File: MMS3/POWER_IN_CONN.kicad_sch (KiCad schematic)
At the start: 1 part, among them J2 AMASS XT60

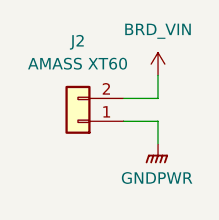
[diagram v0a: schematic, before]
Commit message: schematic + partly layout
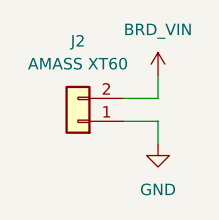
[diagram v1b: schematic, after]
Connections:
- net GNDPWR renamed GND
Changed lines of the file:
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@@
+	)
+	(symbol
+		(lib_id "power:GND")
+		(at 154.94 109.22 0)
+		(unit 1)
+		(body_style 1)
+		(exclude_from_sim no)
+		(in_bom yes)
+		(on_board yes)
+		(in_pos_files yes)
+		(dnp no)
+		(fields_autoplaced yes)
+		(property "Reference" "#PWR059"
+			(at 154.94 115.57 0)
+			(hide yes)
+			(show_name no)
+			(do_not_autoplace no)
+			(effects
+				(font
+					(size 1.27 1.27)
+				)
+			)
+		)
+		(property "Value" "GND"
+			(at 154.94 114.3 0)
+			(show_name no)
+			(do_not_autoplace no)
+			(effects
+				(font
+					(size 1.27 1.27)
+				)
+			)
+		)
+		(property "Footprint" ""
+			(at 154.94 109.22 0)
+			(hide yes)
+			(show_name no)
+			(do_not_autoplace no)
+			(effects
+				(font
+					(size 1.27 1.27)
+				)
+			)
+		)
+		(property "Datasheet" ""
+			(at 154.94 109.22 0)
+			(hide yes)
+			(show_name no)
+			(do_not_autoplace no)
+			(effects
+				(font
+					(size 1.27 1.27)
+				)
+			)
+		)
+		(property "Description" "Power symbol creates a global label with name \"GND\" , ground"
+			(at 154.94 109.22 0)
+			(hide yes)
+			(show_name no)
+			(do_not_autoplace no)
+			(effects
+				(font
+					(size 1.27 1.27)
+				)
+			)
+		)
+		(pin "1"
+		)
+		(instances
+			(project "MMS3"
+				(path "/712cea22-140d-4c92-923f-f4998caf3ecd/e992d219-4a1f-4323-96a2-9f900f6a567a"
+					(reference "#PWR059")
+					(unit 1)
+				)
+			)
+		)
 	)
 	(symbol
@@
 					(unit 1)
 				)
-			)
-		)
-	)
-	(symbol
-		(lib_id "power:GNDPWR")
-		(at 154.94 109.22 0)
-		(unit 1)
-		(body_style 1)
-		(exclude_from_sim no)
-		(in_bom yes)
-		(on_board yes)
-		(in_pos_files yes)
-		(dnp no)
-		(fields_autoplaced yes)
-		(property "Reference" "#PWR024"
-			(at 154.94 114.3 0)
-			(hide yes)
-			(show_name no)
-			(do_not_autoplace no)
-			(effects
-				(font
-					(size 1.27 1.27)
-				)
-			)
-		)
-		(property "Value" "GNDPWR"
-			(at 154.813 113.03 0)
-			(show_name no)
-			(do_not_autoplace no)
-			(effects
-				(font
-					(size 1.27 1.27)
-				)
-			)
-		)
-		(property "Footprint" ""
-			(at 154.94 110.49 0)
-			(hide yes)
-			(show_name no)
-			(do_not_autoplace no)
-			(effects
-				(font
-					(size 1.27 1.27)
-				)
-			)
-		)
-		(property "Datasheet" ""
-			(at 154.94 110.49 0)
-			(hide yes)
-			(show_name no)
-			(do_not_autoplace no)
-			(effects
-				(font
-					(size 1.27 1.27)
-				)
-			)
-		)
-		(property "Description" "Power symbol creates a global label with name \"GNDPWR\" , global ground"
-			(at 154.94 109.22 0)
-			(hide yes)
-			(show_name no)
-			(do_not_autoplace no)
-			(effects
-				(font
-					(size 1.27 1.27)
-				)
-			)
-		)
-		(pin "1"
-		)
-		(instances
-			(project "MMS3"
-				(path "/712cea22-140d-4c92-923f-f4998caf3ecd/e992d219-4a1f-4323-96a2-9f900f6a567a"
-					(reference "#PWR024")
-					(unit 1)
-				)
